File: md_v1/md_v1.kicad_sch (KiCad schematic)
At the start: 18 parts, among them U1 MCT8316Z0TRGFR

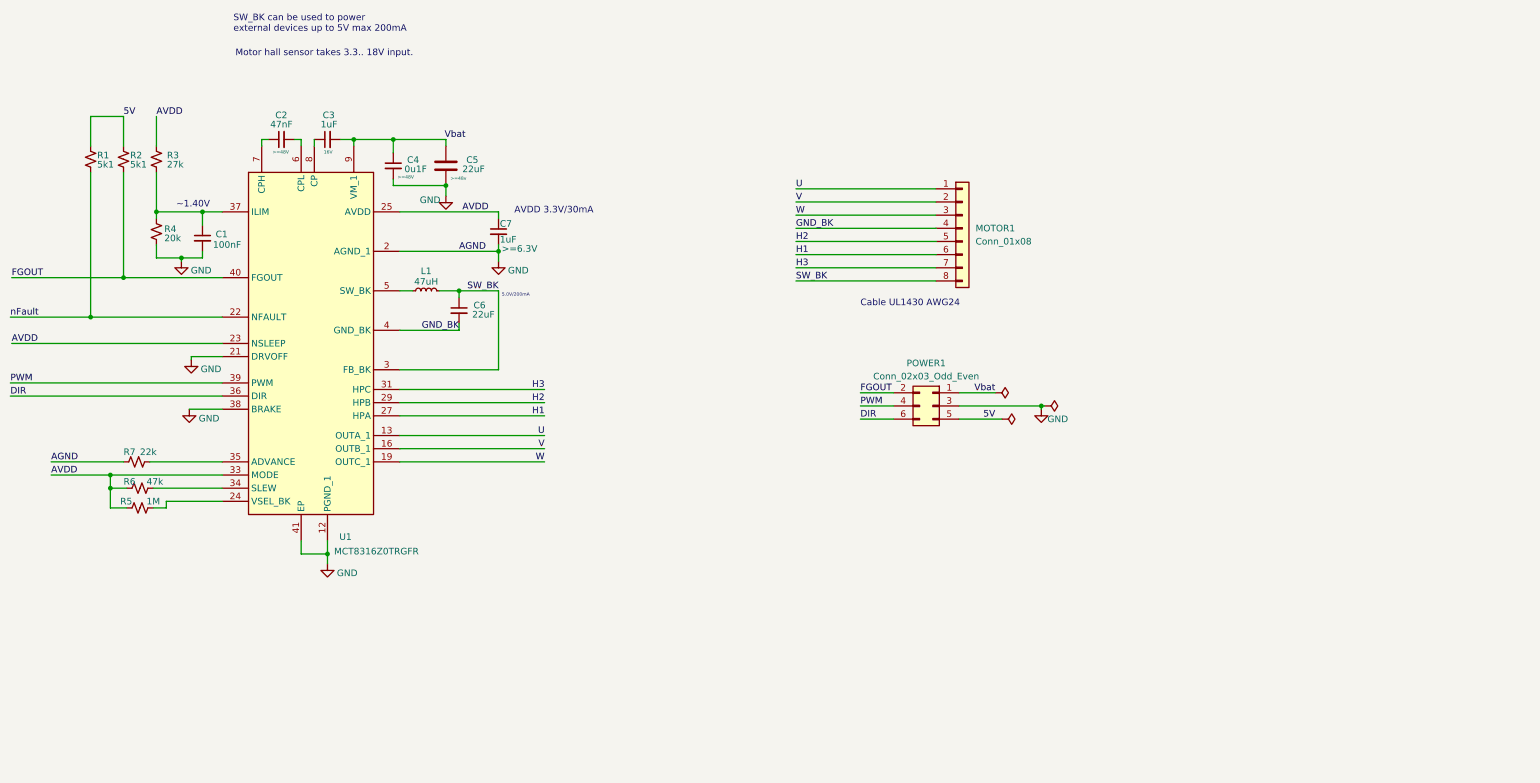
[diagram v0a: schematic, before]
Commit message: File structure enhanced.
Added uniform titleblocks and 3D renders for easier view, file cleanups.
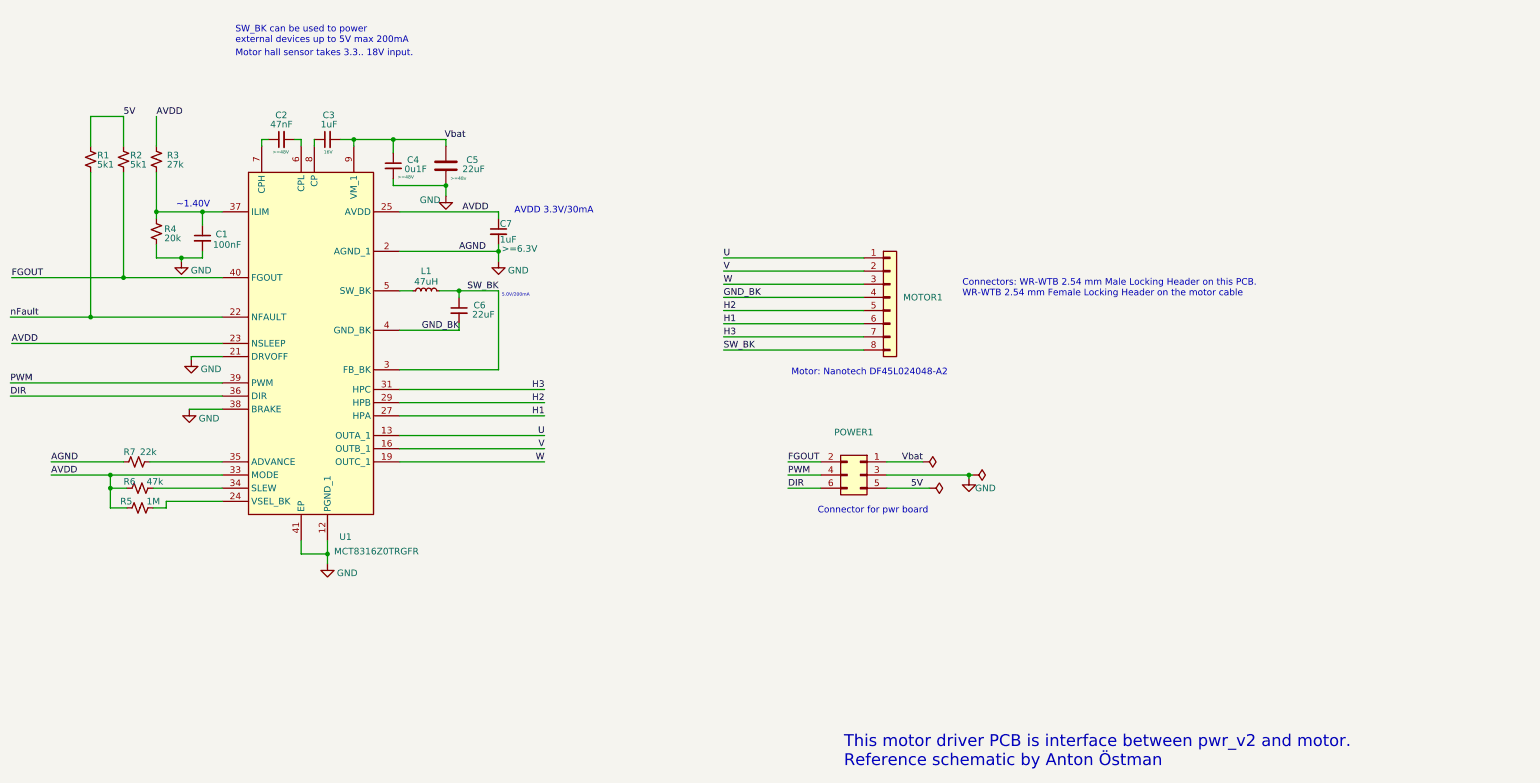
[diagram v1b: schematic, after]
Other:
- note added: "Connector for pwr board"
- note added: "Connectors: WR-WTB 2.54 mm Male Locking Header on this PCB. WR-WTB 2.54 mm Female Locking Header on the motor cable"
- note added: "Motor: Nanotech DF45L024048-A2"
- note added: "This motor driver PCB is interface between pwr_v2 and motor. Reference schematic by Anton Östman"
- note removed: "Cable UL1430 AWG24"
- title: (none) -> Motor driver for pwr_v2
- moved on the sheet: MOTOR1, POWER1
